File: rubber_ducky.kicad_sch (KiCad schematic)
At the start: 3 parts, among them U1 ATmega32U4-A

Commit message: first demo
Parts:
- added C2, C4: 20pF, Capacitor_SMD:C_0805_2012Metric_Pad1.18x1.45mm_HandSolder, symbol Device:C
- added R1, R2: 22Ω, Resistor_SMD:R_0805_2012Metric_Pad1.20x1.40mm_HandSolder, symbol Device:R
- added U2: USB-C-2.0, usb-c-2.0:usb-c-2.0-MODULE, symbol usb-c-2.0:usb_c-2.0-MODULE
- added Y1: ASCO, SMD3225:Crystal_SMD_3225-4Pin_3.2x2.5mm_HandSoldering, symbol Oscillator:ASCO
- renumbered C2 to C3
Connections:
- net GND: now also C2.2, C4.2, U2.4 (V-), Y1.2 (GND)
- net at U1.16 (XTAL2): now also C2.1, Y1.3 (OUT)
- net at U1.17 (XTAL1): now also C4.1, Y1.1 (Tri-State)
- net at U1.3 (D-): now also R2.1
- net at U1.4 (D+): now also R1.1
- net VBUS renamed +5V
- net +5V: now also U2.1 (V+), Y1.4 (VDD)
- new net: R2.2, U2.2 (D-)
- new net: R1.2, U2.3 (D+)

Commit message: hotfix v.02
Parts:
- added R3: 10k, symbol Device:R
- added SW1: SW_MEC_5G, symbol Switch:SW_MEC_5G
- C1: value 1μF -> 1u
- C2, C4: value 20pF -> 20p
- C3: value 10μF -> 10u
- R1, R2: value 22Ω -> 22
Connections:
- net +5V: now also C3.1, R3.1
- net GND: now also SW1.1 (A), SW1.2 (A); no longer C3.1
- net at U1.13 (~{RESET}): now also R3.2, SW1.3 (B), SW1.4 (B)
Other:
- moved on the sheet: C2, C4, Y1

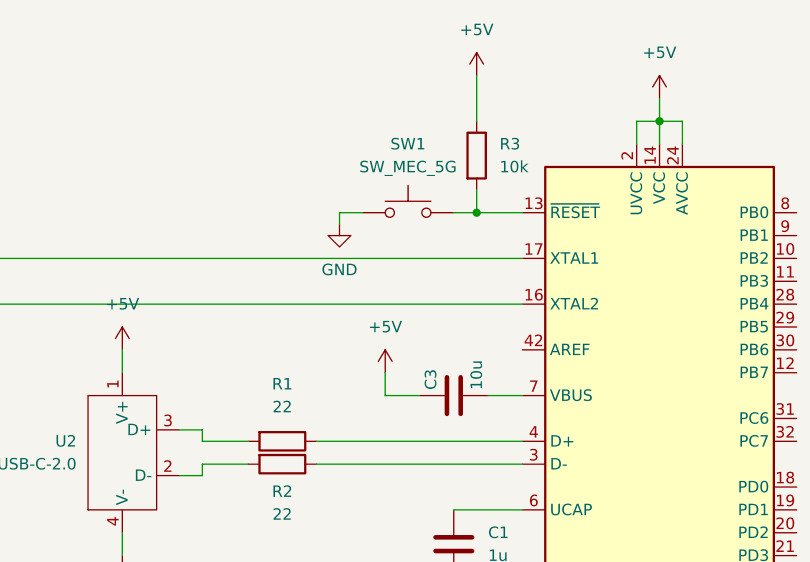
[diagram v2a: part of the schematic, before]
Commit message: rotation of atmega
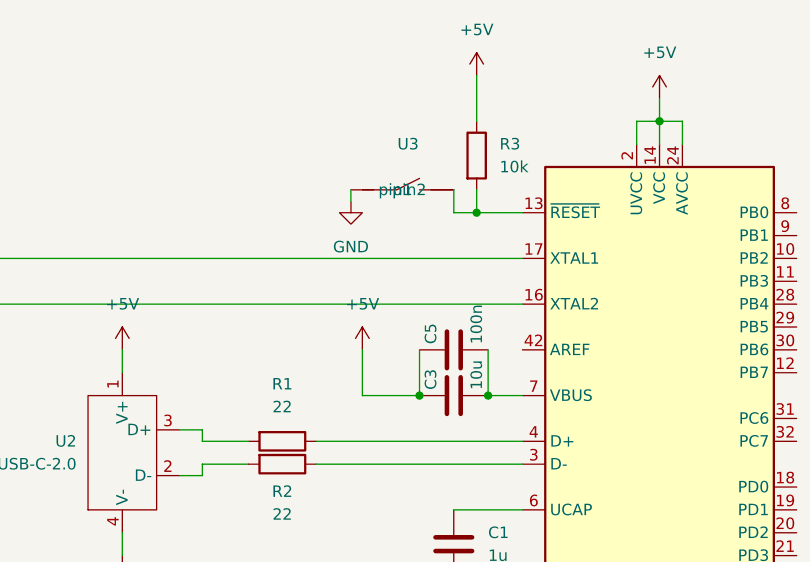
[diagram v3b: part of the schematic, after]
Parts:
- removed SW1: SW_MEC_5G, symbol Switch:SW_MEC_5G
- added C5: 100n, Capacitor_SMD:C_0805_2012Metric_Pad1.18x1.45mm_HandSolder, symbol Device:C
- added U3: ~, usb-c-2.0:switch, symbol usb-c-2.0:switch
- R3: footprint (none) -> Resistor_SMD:R_0805_2012Metric_Pad1.20x1.40mm_HandSolder
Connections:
- net +5V: now also C5.1
- net GND: now also U3. (pin2)
- net at R3.2, U1.13 (~{RESET}): now also U3. (pin2)
- net at C3.2, U1.7 (VBUS): now also C5.2

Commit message: hotfix v0.3
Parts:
- added D1: LED, LED_SMD:LED_0805_2012Metric_Pad1.15x1.40mm_HandSolder, symbol Device:LED
- added R4: 220, Resistor_SMD:R_0805_2012Metric_Pad1.20x1.40mm_HandSolder, symbol Device:R
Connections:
- net GND: now also R4.1
- net at U1.29 (PB5): now also D1.2 (A)
- new net: D1.1 (K), R4.2
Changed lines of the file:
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@@
+	(wire
+		(pts
+			(xy 184.15 74.93) (xy 186.69 74.93)
+		)
+		(stroke
+			(width 0)
+			(type default)
+		)
+	)
 	(wire
 		(pts
@@
 	(wire
 		(pts
+			(xy 194.31 74.93) (xy 198.12 74.93)
+		)
+		(stroke
+			(width 0)
+			(type default)
+		)
+	)
+	(wire
+		(pts
 			(xy 129.54 82.55) (xy 123.19 82.55)
 		)
@@
 	(wire
 		(pts
+			(xy 171.45 74.93) (xy 176.53 74.93)
+		)
+		(stroke
+			(width 0)
+			(type default)
+		)
+	)
+	(wire
+		(pts
 			(xy 96.52 77.47) (xy 96.52 80.01)
 		)
@@
 		(pts
 			(xy 133.35 95.25) (xy 140.97 95.25)
+		)
+		(stroke
+			(width 0)
+			(type default)
+		)
+	)
+	(wire
+		(pts
+			(xy 198.12 74.93) (xy 198.12 76.2)
 		)
 		(stroke
@@
 	)
 	(symbol
+		(lib_id "Device:R")
+		(at 190.5 74.93 270)
+		(unit 1)
+		(exclude_from_sim no)
+		(in_bom yes)
+		(on_board yes)
+		(dnp no)
+		(fields_autoplaced yes)
+		(property "Reference" "R4"
+			(at 190.5 68.58 90)
+			(effects
+				(font
+					(size 1.27 1.27)
+				)
+			)
+		)
+		(property "Value" "220"
+			(at 190.5 71.12 90)
+			(effects
+				(font
+					(size 1.27 1.27)
+				)
+			)
+		)
+		(property "Footprint" "Resistor_SMD:R_0805_2012Metric_Pad1.20x1.40mm_HandSolder"
+			(at 190.5 73.152 90)
+			(effects
+				(font
+					(size 1.27 1.27)
+				)
+				(hide yes)
+			)
+		)
+		(property "Datasheet" "~"
+			(at 190.5 74.93 0)
+			(effects
+				(font
+					(size 1.27 1.27)
+				)
+				(hide yes)
+			)
+		)
+		(property "Description" "Resistor"
+			(at 190.5 74.93 0)
+			(effects
+				(font
+					(size 1.27 1.27)
+				)
+				(hide yes)
+			)
+		)
+		(pin "2"
+		)
+		(pin "1"
+		)
+		(instances
+			(project "rubber_ducky"
+				(path "/0fe84280-f8f9-49bd-b201-ce309d740806"
+					(reference "R4")
+					(unit 1)
+				)
+			)
+		)
+	)
+	(symbol
 		(lib_id "power:VBUS")
 		(at 96.52 77.47 0)
@@
 	)
 	(symbol
+		(lib_id "Device:LED")
+		(at 180.34 74.93 180)
+		(unit 1)
+		(exclude_from_sim no)
+		(in_bom yes)
+		(on_board yes)
+		(dnp no)
+		(fields_autoplaced yes)
+		(property "Reference" "D1"
+			(at 181.9275 67.31 0)
+			(effects
+				(font
+					(size 1.27 1.27)
+				)
+			)
+		)
+		(property "Value" "LED"
+			(at 181.9275 69.85 0)
+			(effects
+				(font
+					(size 1.27 1.27)
+				)
+			)
+		)
+		(property "Footprint" "LED_SMD:LED_0805_2012Metric_Pad1.15x1.40mm_HandSolder"
+			(at 180.34 74.93 0)
+			(effects
+				(font
+					(size 1.27 1.27)
+				)
+				(hide yes)
+			)
+		)
+		(property "Datasheet" "~"
+			(at 180.34 74.93 0)
+			(effects
+				(font
+					(size 1.27 1.27)
+				)
+				(hide yes)
+			)
+		)
+		(property "Description" "Light emitting diode"
+			(at 180.34 74.93 0)
+			(effects
+				(font
+					(size 1.27 1.27)
+				)
+				(hide yes)
+			)
+		)
+		(property "Sim.Pins" "1=K 2=A"
+			(at 180.34 74.93 0)
+			(effects
+				(font
+					(size 1.27 1.27)
+				)
+				(hide yes)
+			)
+		)
+		(pin "1"
+		)
+		(pin "2"
+		)
+		(instances
+			(project ""
+				(path "/0fe84280-f8f9-49bd-b201-ce309d740806"
+					(reference "D1")
+					(unit 1)
+				)
+			)
+		)
+	)
+	(symbol
 		(lib_id "power:PWR_FLAG")
 		(at 137.16 124.46 0)
@@
 					(unit 1)
 				)
+			)
+		)
+	)
+	(symbol
+		(lib_id "power:GND")
+		(at 198.12 76.2 0)
+		(unit 1)
+		(exclude_from_sim no)
+		(in_bom yes)
+		(on_board yes)
+		(dnp no)
+		(fields_autoplaced yes)
+		(property "Reference" "#PWR016"
+			(at 198.12 82.55 0)
+			(effects
+				(font
+					(size 1.27 1.27)
+				)
+				(hide yes)
+			)
+		)
+		(property "Value" "GND"
+			(at 198.12 81.28 0)
+			(effects
+				(font
+					(size 1.27 1.27)
+				)
+			)
+		)
+		(property "Footprint" ""
+			(at 198.12 76.2 0)
+			(effects
+				(font
+					(size 1.27 1.27)
+				)
+				(hide yes)
+			)
+		)
+		(property "Datasheet" ""
+			(at 198.12 76.2 0)
+			(effects
+				(font
+					(size 1.27 1.27)
+				)
+				(hide yes)
+			)
+		)
+		(property "Description" "Power symbol creates a global label with name \"GND\" , ground"
+			(at 198.12 76.2 0)
+			(effects
+				(font
+					(size 1.27 1.27)
+				)
+				(hide yes)
+			)
+		)
+		(pin "1"
+		)
+		(instances
+			(project "rubber_ducky"
+				(path "/0fe84280-f8f9-49bd-b201-ce309d740806"
+					(reference "#PWR016")
+					(unit 1)
+				)

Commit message: v2
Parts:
- Y1: footprint SMD3225:Crystal_SMD_3225-4Pin_3.2x2.5mm_HandSoldering -> Crystal:Crystal_SMD_3225-4Pin_3.2x2.5mm_HandSoldering
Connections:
- net GND: now also U3.1; no longer U3. (pin2)
- net at R3.2, U1.13 (~{RESET}): now also U3.2; no longer U3. (pin2)
- net D1-: now reaches R2.1, U1.3 (D-)
- net D1+: now reaches R1.1, U1.4 (D+)
- net D-: now reaches R2.2, U2.2 (D-)
- net D+: now reaches R1.2, U2.3 (D+)
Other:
- moved on the sheet: U3
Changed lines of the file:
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@@
+	(wire
+		(pts
+			(xy 121.92 59.69) (xy 123.19 59.69)
+		)
+		(stroke
+			(width 0)
+			(type default)
+		)
+	)
 	(wire
 		(pts
@@
 			(width 0)
 			(type default)
+		)
+	)
+	(label "D+"
+		(at 106.68 87.63 0)
+		(effects
+			(font
+				(size 1.27 1.27)
+			)
+			(justify left bottom)
+		)
+	)
+	(label "D1-"
+		(at 123.19 90.17 0)
+		(effects
+			(font
+				(size 1.27 1.27)
+			)
+			(justify left bottom)
+		)
+	)
+	(label "D-"
+		(at 107.95 90.17 0)
+		(effects
+			(font
+				(size 1.27 1.27)
+			)
+			(justify left bottom)
+		)
+	)
+	(label "D1+"
+		(at 123.19 87.63 0)
+		(effects
+			(font
+				(size 1.27 1.27)
+			)
+			(justify left bottom)
 		)
 	)
@@
 			)
 		)
-		(property "Footprint" "SMD3225:Crystal_SMD_3225-4Pin_3.2x2.5mm_HandSoldering"
+		(property "Footprint" "Crystal:Crystal_SMD_3225-4Pin_3.2x2.5mm_HandSoldering"
 			(at 60.96 69.85 0)
 			(effects
@@
 			)
 		)
-		(pin ""
-		)
-		(pin ""
-		)
-		(instances
+		(pin "1"
+		)
+		(pin "2"
+		)
+		(instances
